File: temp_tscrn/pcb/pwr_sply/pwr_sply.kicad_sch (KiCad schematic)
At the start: 9 parts, among them J1 Screw_Terminal_01x03, J2 Conn_01x03_Male, Q1 Q_PMOS_GSD

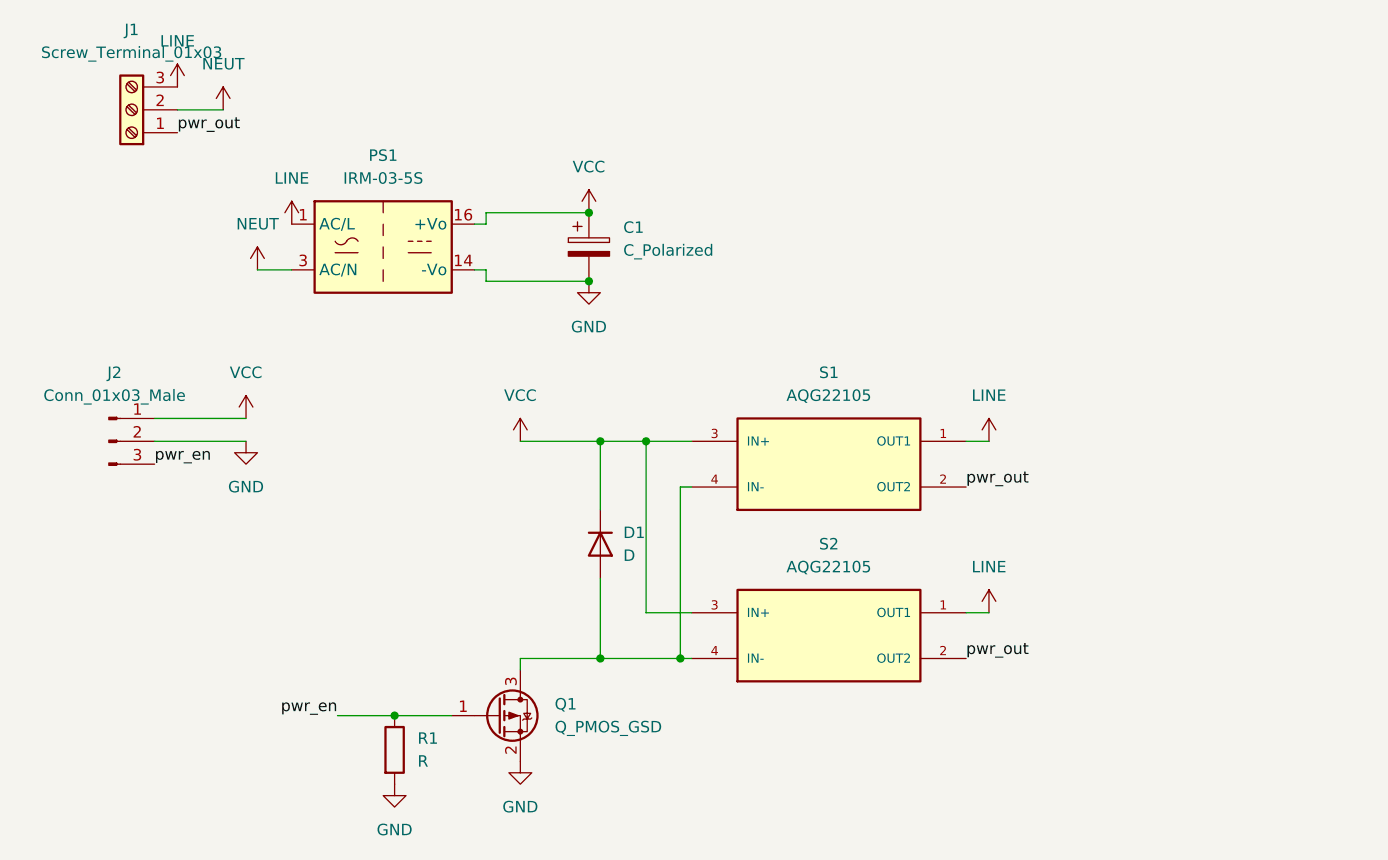
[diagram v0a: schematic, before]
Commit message: temp_tscrn: pcb: add ldo
Add LDO in the power supply board for compatibility with the display
board. Max current for LDO is 450 mA. The MOSFET should be fine if
controlled with 3.3V switching 5V for SSR control.
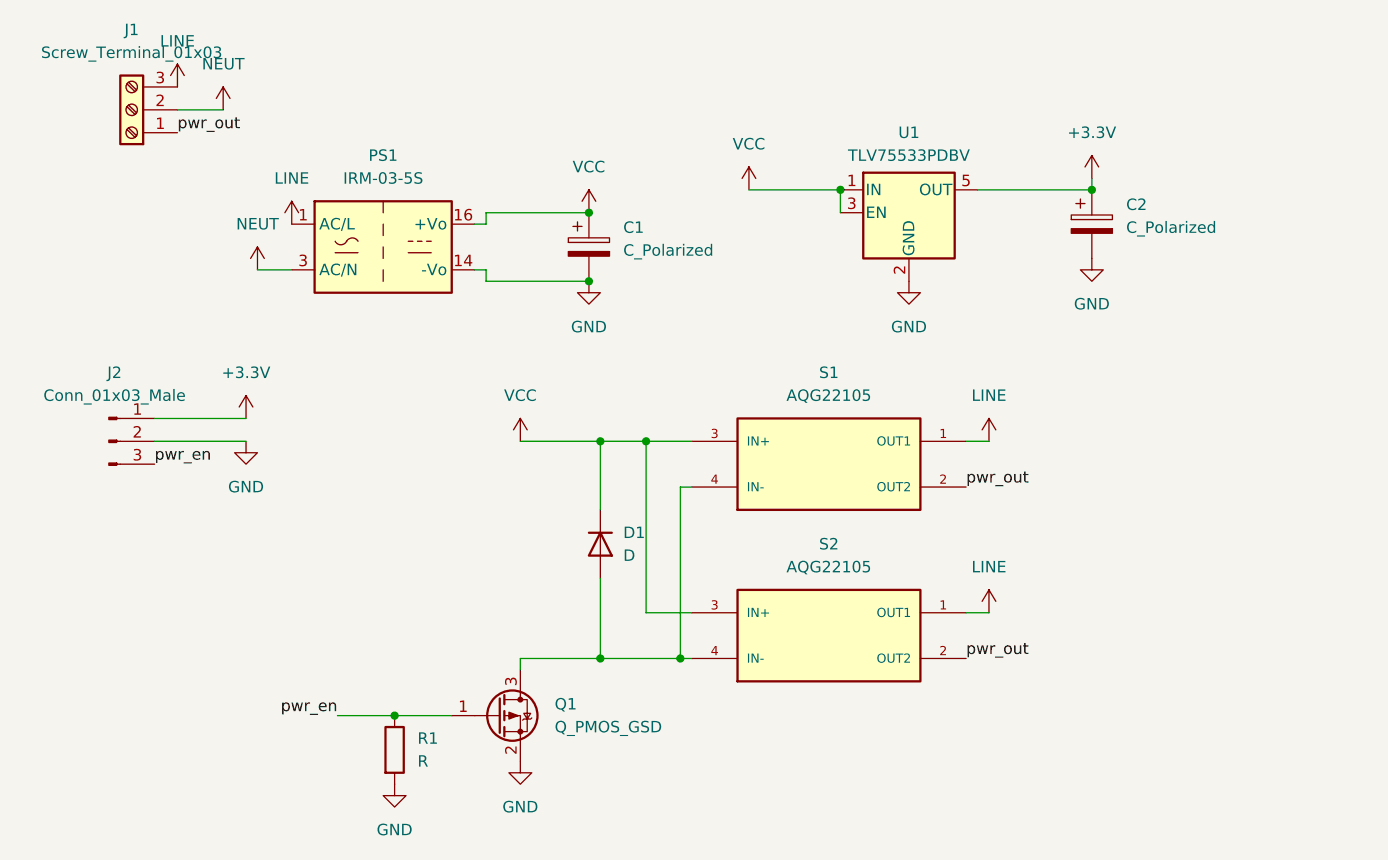
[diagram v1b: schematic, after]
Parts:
- added C2: C_Polarized, Capacitor_Tantalum_SMD:CP_EIA-3216-18_Kemet-A_Pad1.58x1.35mm_HandSolder, symbol Device:C_Polarized
- added U1: TLV75533PDBV, Package_TO_SOT_SMD:SOT-23-5, symbol Regulator_Linear:TLV75533PDBV
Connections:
- net GND: now also C2.2, U1.2 (GND)
- net VCC: now also U1.1 (IN), U1.3 (EN); no longer J2.1 (Pin_1)
- new net +3.3V: C2.1, J2.1 (Pin_1), U1.5 (OUT)

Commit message: temp_tscrn: pcb v3
Version 3 of power supply for temp_tscrn PCB. This one uses triac and
optotriac to control the heater
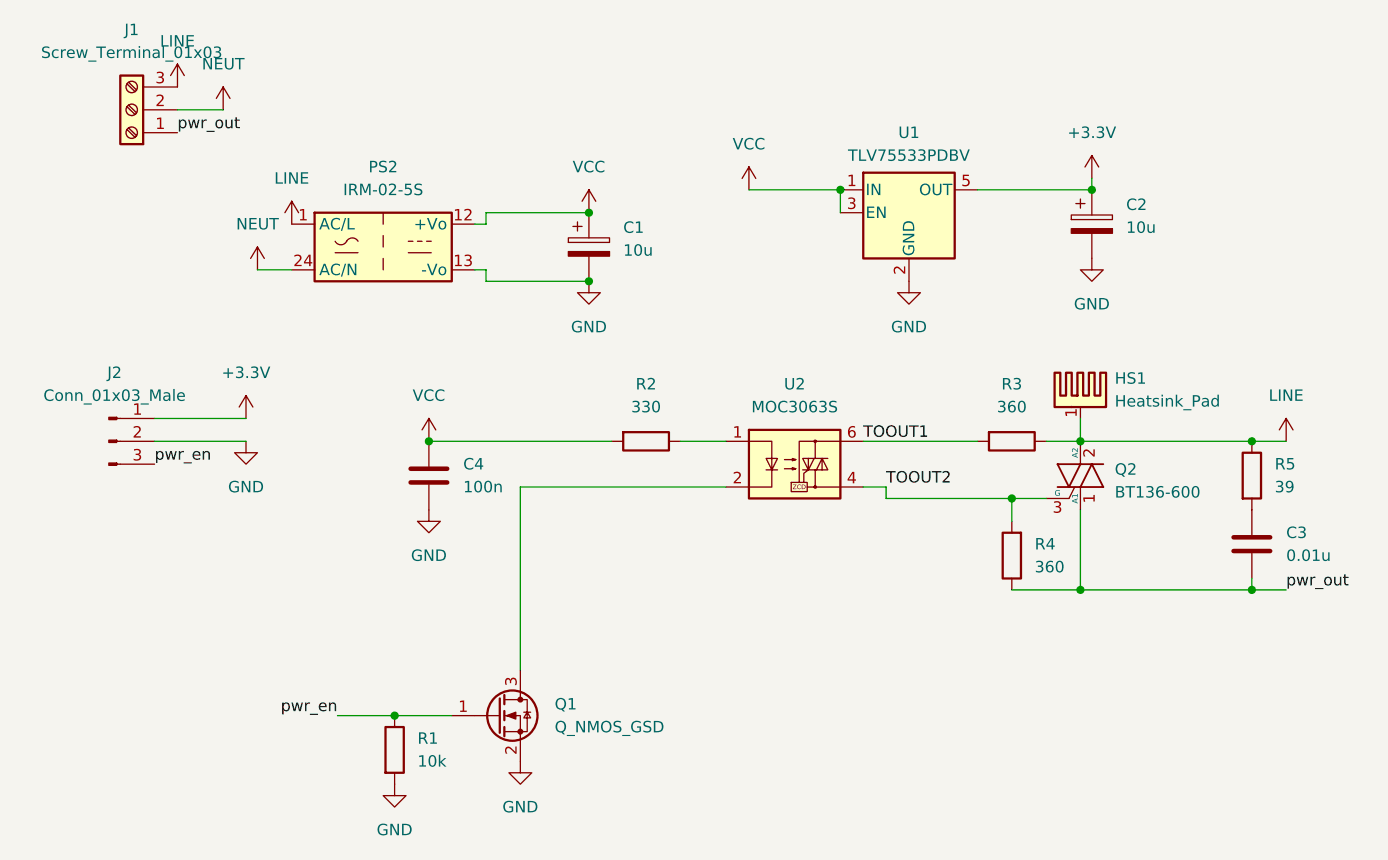
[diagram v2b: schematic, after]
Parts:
- removed D1: D, Diode_SMD:D_SOD-123, symbol Device:D
- removed PS1: IRM-03-5S, Converter_ACDC:Converter_ACDC_MeanWell_IRM-03-xx_SMD, symbol Converter_ACDC:IRM-03-3.3S
- removed Q1: Q_PMOS_GSD, Package_TO_SOT_SMD:SOT-23, symbol Device:Q_PMOS_GSD
- removed S1, S2: AQG22105, pwr_sply:RELAY_AQG22105, symbol AQG22105:AQG22105
- added C3: 0.01u, Capacitor_THT:C_Rect_L10.0mm_W5.0mm_P5.00mm_P7.50mm, symbol Device:C
- added C4: 100n, Capacitor_SMD:C_0603_1608Metric_Pad1.08x0.95mm_HandSolder, symbol Device:C
- added HS1: Heatsink_Pad, symbol Mechanical:Heatsink_Pad
- added PS2: IRM-02-5S, Converter_ACDC:Converter_ACDC_MeanWell_IRM-02-xx_SMD, symbol Converter_ACDC:IRM-02-5S
- added Q1: Q_NMOS_GSD, Package_TO_SOT_SMD:SOT-23, symbol Transistor_FET:Q_NMOS_GSD
- added Q2: BT136-600, Package_TO_SOT_SMD:TO-252-2, symbol Triac_Thyristor:BT136-600
- added R2: 330, Resistor_SMD:R_0603_1608Metric_Pad0.98x0.95mm_HandSolder, symbol Device:R
- added R3, R4: 360, Resistor_SMD:R_0603_1608Metric_Pad0.98x0.95mm_HandSolder, symbol Device:R
- added R5: 39, Resistor_SMD:R_0603_1608Metric_Pad0.98x0.95mm_HandSolder, symbol Device:R
- added U2: MOC3063S, Package_DIP:SMDIP-6_W7.62mm, symbol Relay_SolidState:MOC3063M
- C1, C2: value C_Polarized -> 10u
- R1: value R -> 10k
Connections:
- net GND: now also C4.2, PS2.13 (-Vo), Q1.2 (S)
- net LINE: now also HS1.1, PS2.1 (AC/L), Q2.2 (A2), R3.1, R5.1
- net NEUT: now also PS2.24 (AC/N)
- net VCC: now also C4.1, PS2.12 (+Vo), R2.2
- net pwr_en: now also Q1.1 (G)
- net pwr_out: now also C3.2, Q2.1 (A1), R4.1
- new net: C3.1, R5.2
- new net: R2.1, U2.1
- new net: Q1.3 (D), U2.2
- new net TOOUT1: R3.2, U2.6
- new net TOOUT2: Q2.3 (G), R4.2, U2.4
